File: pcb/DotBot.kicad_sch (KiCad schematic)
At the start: 65 parts, among them J1 Shield Header, J10 Extra Pins, J11 Motor connector, J12 Motor connector, J6 SWD, J7 Shield Header, J8 Extra Pins, J9 Extra Pins, Q1 DMN62D0U-7, Q2 DMG2301L-7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

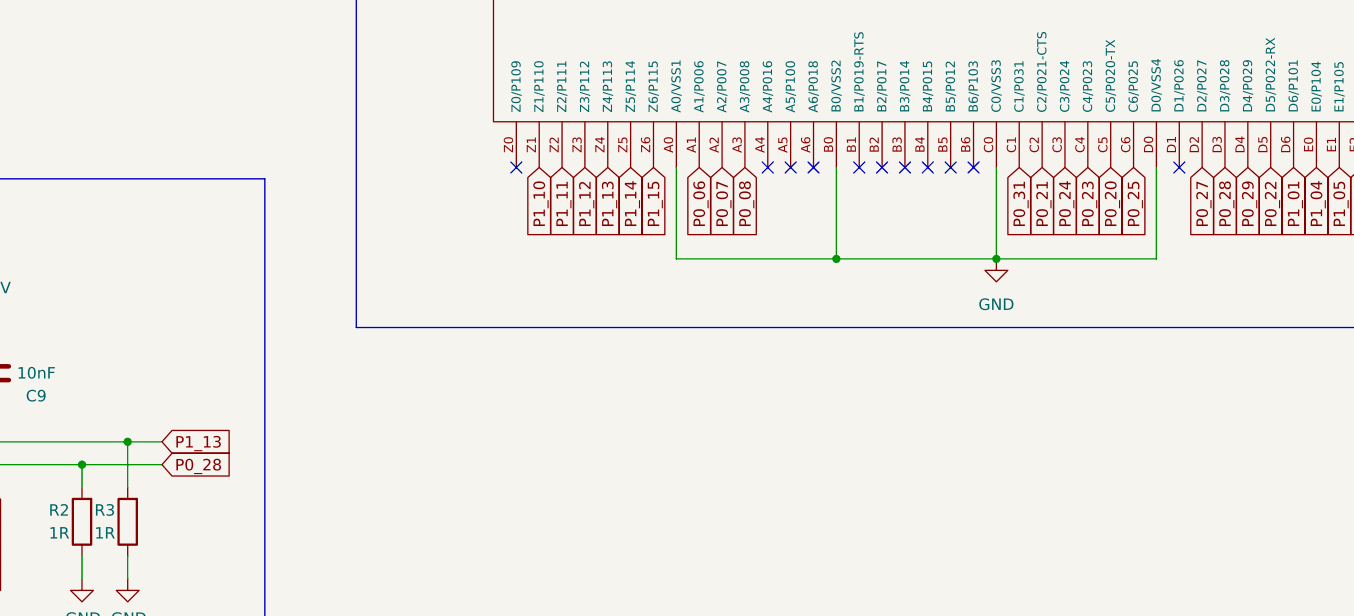
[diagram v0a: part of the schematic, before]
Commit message: DotBot: use P0.26 for AISEN motor driver
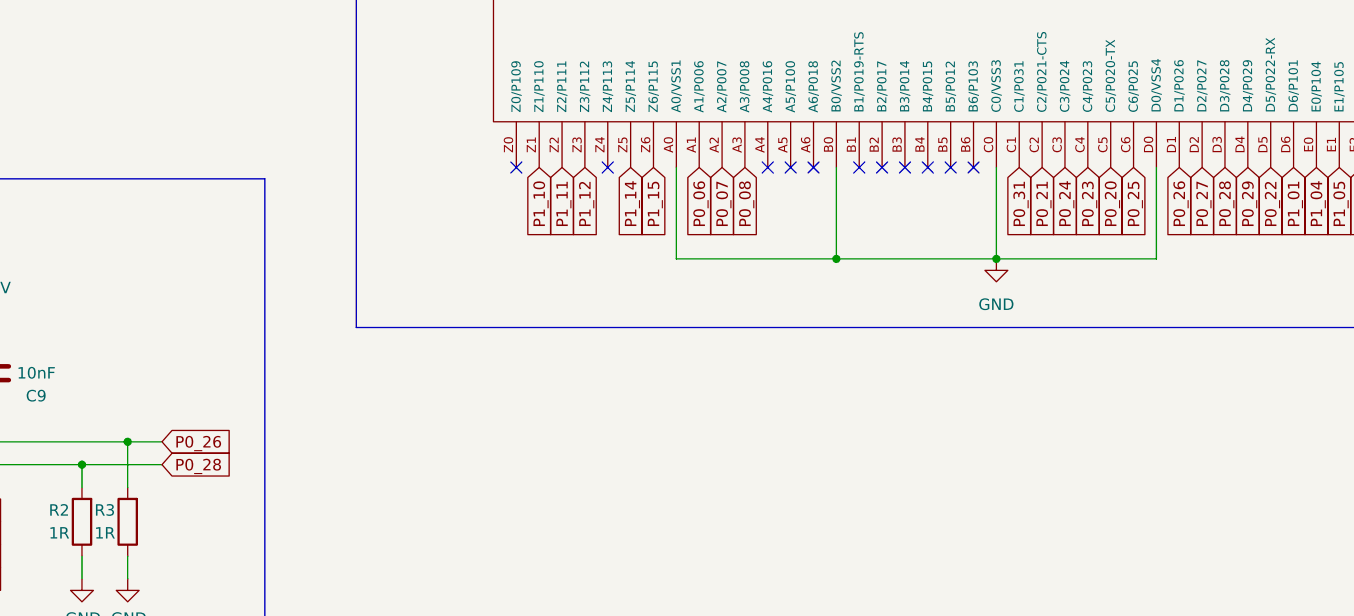
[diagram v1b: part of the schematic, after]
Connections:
- net P0_26: now reaches U7.D1 (D1/P026)
- net P0_26: now also R3.2, U3.3 (AISEN)
- removed net P1_13: R3.2, U3.3 (AISEN), U7.Z4 (Z4/P113)
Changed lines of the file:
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@@
   )
   (no_connect (at 222.25 139.7))
-  (no_connect (at 245.11 139.7))
+  (no_connect (at 181.61 139.7))
   (no_connect (at 209.55 139.7))
   (no_connect (at 217.17 139.7))
@@
     )
   )
+  (global_label "P0_26" (shape input) (at 245.11 139.7 270) (fields_autoplaced)
+    (effects (font (size 1.27 1.27)) (justify right))
+    (property "Intersheetrefs" "${INTERSHEET_REFS}" (at 245.11 148.5513 90)
+      (effects (font (size 1.27 1.27)) (justify right) hide)
+    )
+  )
   (global_label "P0_05" (shape input) (at 77.47 39.37 0) (fields_autoplaced)
     (effects (font (size 1.27 1.27)) (justify left))
@@
     )
   )
-  (global_label "P1_13" (shape input) (at 132.08 170.18 0) (fields_autoplaced)
-    (effects (font (size 1.27 1.27)) (justify left))
-    (property "Intersheetrefs" "${INTERSHEET_REFS}" (at 140.8519 170.18 0)
-      (effects (font (size 1.27 1.27)) (justify left) hide)
-    )
-  )
-  (global_label "P1_13" (shape input) (at 181.61 139.7 270) (fields_autoplaced)
-    (effects (font (size 1.27 1.27)) (justify right))
-    (property "Intersheetrefs" "${INTERSHEET_REFS}" (at 181.61 148.4719 90)
-      (effects (font (size 1.27 1.27)) (justify right) hide)
-    )
-  )
+  (global_label "P0_26" (shape input) (at 132.08 170.18 0) (fields_autoplaced)
+    (effects (font (size 1.27 1.27)) (justify left))
+    (property "Intersheetrefs" "${INTERSHEET_REFS}" (at 140.9313 170.18 0)
+      (effects (font (size 1.27 1.27)) (justify left) hide)
+    )
+  )

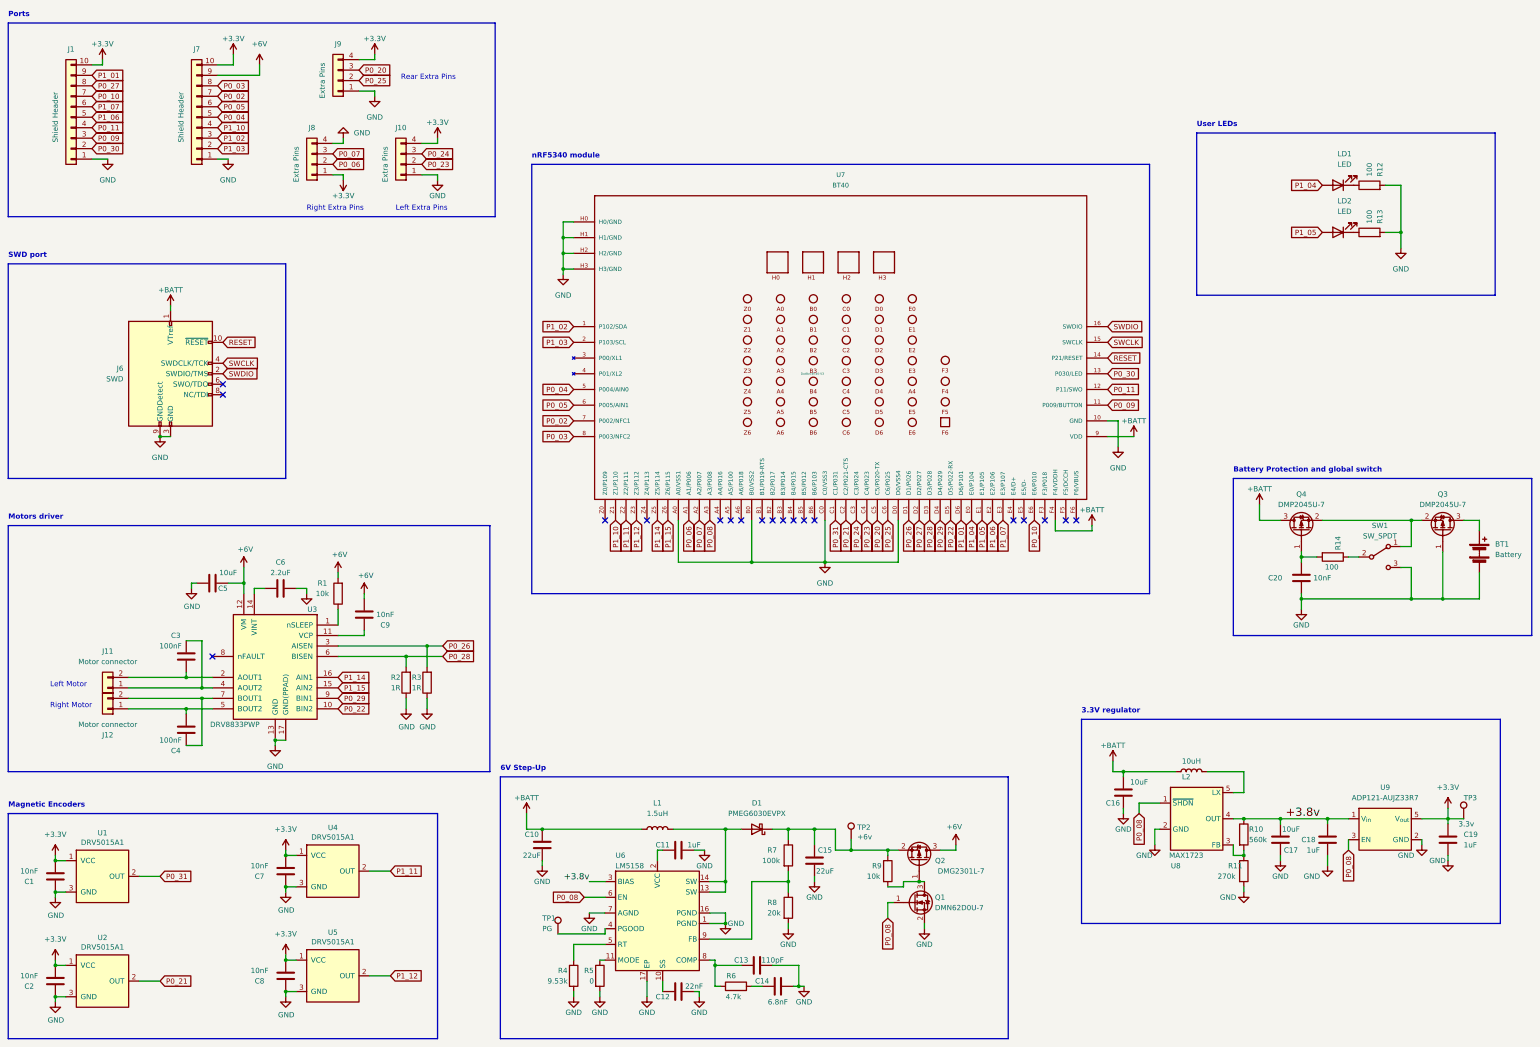
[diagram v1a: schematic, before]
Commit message: doc: update BOM prices
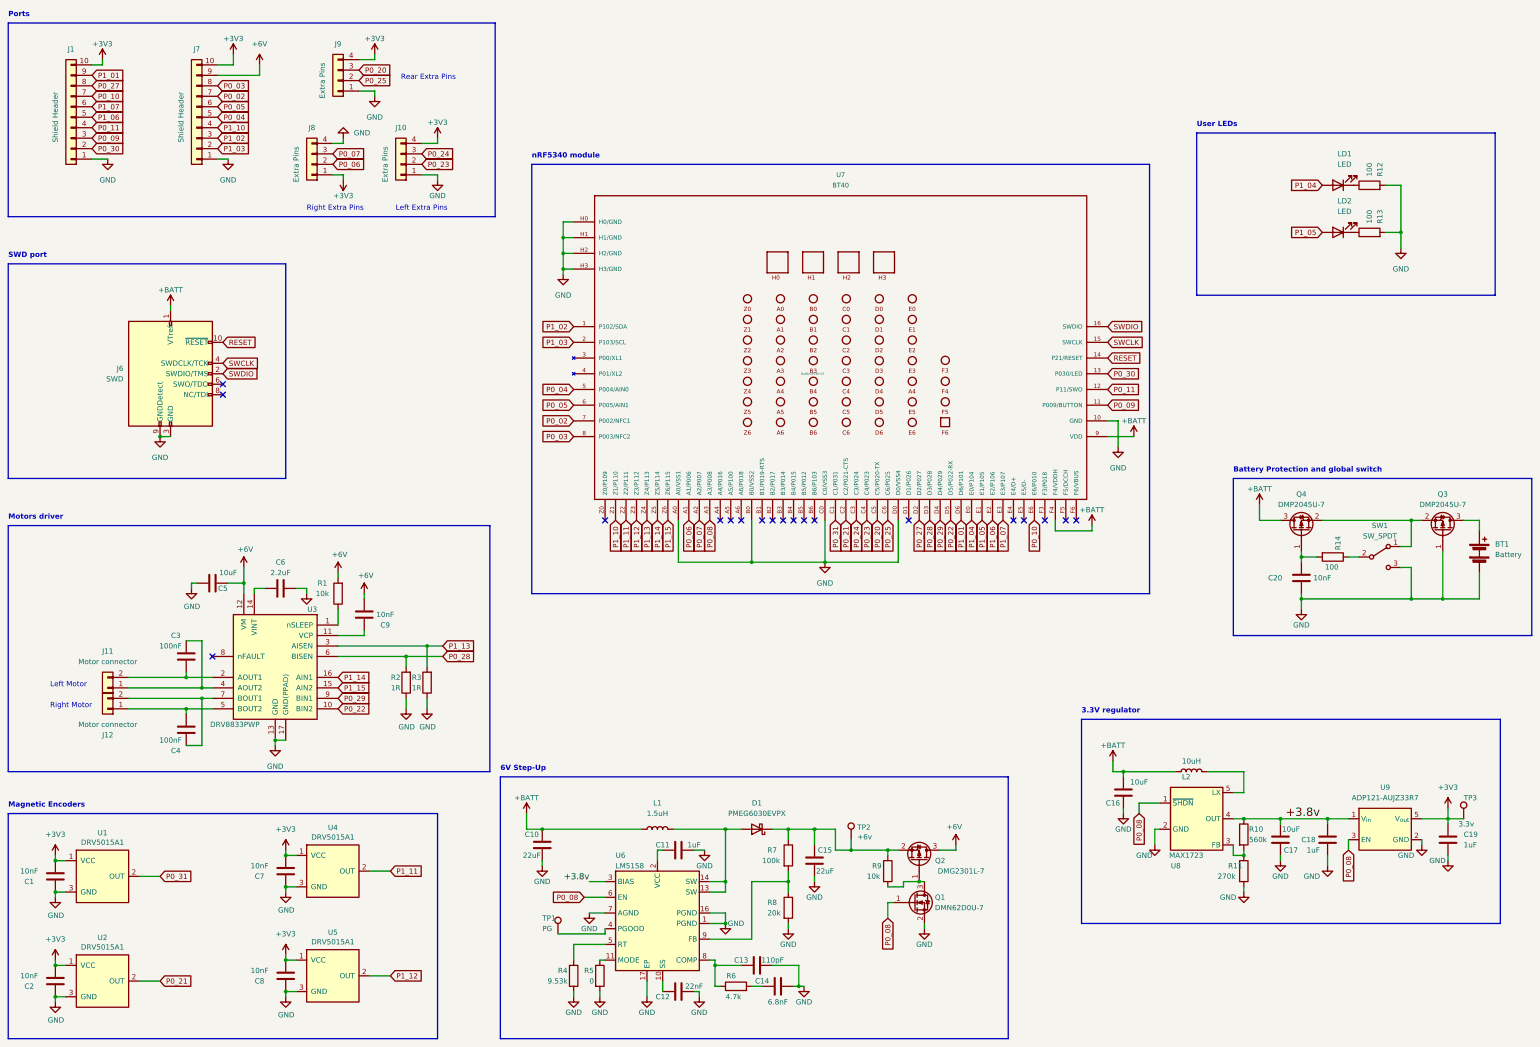
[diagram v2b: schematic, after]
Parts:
- BT1: Price 0.833 -> 0.772
- C1, C2, C20, C7, C8, C9: Price 0.013 -> 0.0127
- C10, C15: Price 0.082 -> 0.059
- C11, C18, C19: Price 0.0085 -> 0.0115
- C12: Price 0.0149 -> 0.0107
- C13: Price 0.125 -> 0.08094
- C14: Price 0.019 -> 0.0175
- C16, C17, C5: Price 0.085 -> 0.042
- C3, C4: Price 0.005 -> 0.0046
- C6: Price 0.056 -> 0.051
- D1: Price 0.189 -> 0.170
- J1, J7: Price 2.738 -> 1.875
- J11, J12: Price 0.067 -> 0.078
- J6: Price 2.167 -> 1.25
- L1: Price 0.128 -> 0.119
- L2: Price 0.127 -> 0.08
- LD1, LD2: Price 0.062 -> 0.066
- Q1: Price 0.067 -> 0.06
- Q2: Price 0.069 -> 0.061
- Q3, Q4: Price 0.10 -> 0.094
- R1, R9: Price 0.0043 -> 0.0053
- R10: Price 0.006 -> 0.0029
- R11: Price 0.006 -> 0.0062
- R12, R13, R14: Price 0.006 -> 0.0063
- R2, R3: Price 0.0087 -> 0.0066
- R4, R7: Price 0.034 -> 0.0354
- R5: Price 0.0037 -> 0.0038
- R6: Price 0.007 -> 0.0053
- R8: Price 0.048 -> 0.0469
- SW1: Price 0.568 -> 0.6528
- U1, U2, U4, U5: Price 0.25 -> 0.29
- U3: Price 1.48 -> 1.22
- U6: Price 2.79 -> 2.25
- U7: Price 9.97 -> 8.704
- U8: Price 2.46 -> 2.24
- U9: Price 0.626 -> 0.635
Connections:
- net P1_13: now reaches U7.Z4 (Z4/P113)
- net P1_13: now also R3.2, U3.3 (AISEN)
- removed net P0_26: R3.2, U3.3 (AISEN), U7.D1 (D1/P026)
